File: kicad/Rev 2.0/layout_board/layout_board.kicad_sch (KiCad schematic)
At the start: 144 parts, among them U0:0 GH39FKSW, U0:1 GH39FKSW, U0:10 GH39FKSW, U0:11 GH39FKSW, U0:12 GH39FKSW, U0:13 GH39FKSW, U0:14 GH39FKSW, U0:2 GH39FKSW, U0:3 GH39FKSW, U0:4 GH39FKSW, U0:5 GH39FKSW, U0:6 GH39FKSW, U0:7 GH39FKSW, U0:8 GH39FKSW, U0:9 GH39FKSW, U1 CD4067BPWR, U1:0 GH39FKSW, U1:1 GH39FKSW, U1:10 GH39FKSW, U1:11 GH39FKSW, U1:12 GH39FKSW, U1:13 GH39FKSW, U1:14 GH39FKSW, U1:2 GH39FKSW, U1:3 GH39FKSW, U1:4 GH39FKSW, U1:5 GH39FKSW, U1:6 GH39FKSW, U1:7 GH39FKSW, U1:8 GH39FKSW, U1:9 GH39FKSW, U2 CD4067BPWR, U2:0 GH39FKSW, U2:1 GH39FKSW, U2:10 GH39FKSW, U2:11 GH39FKSW, U2:12 GH39FKSW, U2:13 GH39FKSW, U2:2 GH39FKSW, U2:3 GH39FKSW, U2:4 GH39FKSW, U2:5 GH39FKSW, U2:6 GH39FKSW, U2:7 GH39FKSW, U2:8 GH39FKSW, U2:9 GH39FKSW, U3 CD4067BPWR, U3:1 GH39FKSW, U3:10 GH39FKSW, U3:11 GH39FKSW, U3:12 GH39FKSW, U3:13 GH39FKSW, U3:2 GH39FKSW, U3:3 GH39FKSW, U3:4 GH39FKSW, U3:5 GH39FKSW, U3:6 GH39FKSW, U3:7 GH39FKSW, U3:8 GH39FKSW, U3:9 GH39FKSW, U4 CD4067BPWR, U4:1 GH39FKSW, U4:10 GH39FKSW, U4:12 GH39FKSW, U4:13 GH39FKSW, U4:14 GH39FKSW, U4:2 GH39FKSW, U4:3 GH39FKSW, U4:5 GH39FKSW, U4:7 GH39FKSW, U4:9 GH39FKSW, U5 CD4067BPWR

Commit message: wip: rev 2.0 pcb
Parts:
- removed C1, C10, C11, C12, C13, C14, C15, C16, C17, C18, C19, C2, C20, C21, C22, C23, C24, C25, C26, C27, C28, C29, C3, C30, C31, C32, C33, C34, C35, C36, C37, C38, C39, C4, C40, C41, C42, C43, C44, C45, C46, C47, C48, C49, C5, C50, C51, C52, C53, C54, C55, C56, C57, C58, C59, C6, C60, C61, C62, C63, C64, C65, C66, C67, C7, C8, C9: 100n, Capacitor_SMD:C_0402_1005Metric_Pad0.74x0.62mm_HandSolder, symbol Device:C
- added J1: Conn_01x12_Socket, symbol Connector:Conn_01x12_Socket
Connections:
- net +3.3VA: now also J1.11 (Pin_11)
- net ADC0: now also J1.10 (Pin_10)
- net ADC1: now also J1.9 (Pin_9)
- net ADC2: now also J1.8 (Pin_8)
- net ADC3: now also J1.7 (Pin_7)
- net ADC4: now also J1.6 (Pin_6)
- net AMUX0:0: now also U3:1.2 (VOUT)
- net AMUX0:1: now also U2:1.2 (VOUT)
- net AMUX0:10: now also U0:0.2 (VOUT)
- net AMUX0:11: now also U1:0.2 (VOUT)
- net AMUX0:12: now also U2:0.2 (VOUT)
- net AMUX0:13: now also U4:1.2 (VOUT)
- net AMUX0:2: now also U3:2.2 (VOUT)
- net AMUX0:3: now also U4:2.2 (VOUT)
- net AMUX0:4: now also U2:2.2 (VOUT)
- net AMUX0:5: now also U1:2.2 (VOUT)
- net AMUX0:6: now also U0:3.2 (VOUT)
- net AMUX0:7: now also U0:2.2 (VOUT)
- net AMUX0:8: now also U1:1.2 (VOUT)
- net AMUX0:9: now also U0:1.2 (VOUT)
- net GND: now also J1.12 (Pin_12)
- net SELECT0: now also J1.4 (Pin_4)
- net SELECT1: now also J1.3 (Pin_3)
- net SELECT2: now also J1.2 (Pin_2)
- net SELECT3: now also J1.1 (Pin_1)
- net AMUX0:14: no longer names the net of U1.17 (14)
- net AMUX0:15: no longer names the net of U1.16 (15)
- net AMUX1:13: no longer names the net of U2.18 (13)
- net AMUX1:14: no longer names the net of U2.17 (14)
- net AMUX1:15: no longer names the net of U2.16 (15)
- net AMUX2:13: no longer names the net of U3.18 (13)
- net AMUX2:14: no longer names the net of U3.17 (14)
- net AMUX2:15: no longer names the net of U3.16 (15)
- net AMUX3:13: no longer names the net of U4.18 (13)
- net AMUX3:14: no longer names the net of U4.17 (14)
- net AMUX3:15: no longer names the net of U4.16 (15)
- net AMUX4:14: no longer names the net of U5.17 (14)
- net AMUX4:15: no longer names the net of U5.16 (15)
- no-connect marks 0 -> 13

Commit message: wip: rev 2.0 pcb
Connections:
- net AMUX0:0: now also U0:1.2 (VOUT); no longer U3:1.2 (VOUT)
- net AMUX0:1: now also U0:0.2 (VOUT); no longer U2:1.2 (VOUT)
- net AMUX0:10: now also U1:2.2 (VOUT); no longer U0:0.2 (VOUT)
- net AMUX0:11: now also U2:2.2 (VOUT); no longer U1:0.2 (VOUT)
- net AMUX0:12: now also U0:3.2 (VOUT); no longer U2:0.2 (VOUT)
- net AMUX0:13: now also U0:2.2 (VOUT); no longer U4:1.2 (VOUT)
- net AMUX0:2: now also U1:0.2 (VOUT); no longer U3:2.2 (VOUT)
- net AMUX0:3: now also U2:0.2 (VOUT); no longer U4:2.2 (VOUT)
- net AMUX0:4: now also U4:1.2 (VOUT); no longer U2:2.2 (VOUT)
- net AMUX0:5: now also U3:1.2 (VOUT); no longer U1:2.2 (VOUT)
- net AMUX0:6: now also U2:1.2 (VOUT); no longer U0:3.2 (VOUT)
- net AMUX0:7: now also U1:1.2 (VOUT); no longer U0:2.2 (VOUT)
- net AMUX0:8: now also U3:2.2 (VOUT); no longer U1:1.2 (VOUT)
- net AMUX0:9: now also U4:2.2 (VOUT); no longer U0:1.2 (VOUT)
- net AMUX1:0: now also U0:4.2 (VOUT)
- net AMUX1:1: now also U3:3.2 (VOUT)
- net AMUX1:10: now also U1:5.2 (VOUT)
- net AMUX1:11: now also U2:5.2 (VOUT)
- net AMUX1:12: now also U0:5.2 (VOUT)
- net AMUX1:2: now also U1:3.2 (VOUT)
- net AMUX1:3: now also U2:3.2 (VOUT)
- net AMUX1:4: now also U4:3.2 (VOUT)
- net AMUX1:5: now also U3:4.2 (VOUT)
- net AMUX1:6: now also U2:4.2 (VOUT)
- net AMUX1:7: now also U1:4.2 (VOUT)
- net AMUX1:8: now also U3:5.2 (VOUT)
- net AMUX1:9: now also U4:5.2 (VOUT)
- net AMUX2:0: now also U0:7.2 (VOUT)
- net AMUX2:1: now also U0:6.2 (VOUT)
- net AMUX2:10: now also U1:8.2 (VOUT)
- net AMUX2:11: now also U2:8.2 (VOUT)
- net AMUX2:12: now also U0:8.2 (VOUT)
- net AMUX2:2: now also U3:6.2 (VOUT)
- net AMUX2:3: now also U1:6.2 (VOUT)
- net AMUX2:4: now also U2:6.2 (VOUT)
- net AMUX2:5: now also U3:7.2 (VOUT)
- net AMUX2:6: now also U2:7.2 (VOUT)
- net AMUX2:7: now also U1:7.2 (VOUT)
- net AMUX2:8: now also U3:8.2 (VOUT)
- net AMUX2:9: now also U4:7.2 (VOUT)
- net AMUX3:0: now also U0:10.2 (VOUT)
- net AMUX3:1: now also U0:9.2 (VOUT)
- net AMUX3:10: now also U4:10.2 (VOUT)
- net AMUX3:11: now also U1:11.2 (VOUT)
- net AMUX3:12: now also U0:11.2 (VOUT)
- net AMUX3:2: now also U3:9.2 (VOUT)
- net AMUX3:3: now also U1:9.2 (VOUT)
- net AMUX3:4: now also U2:9.2 (VOUT)
- net AMUX3:5: now also U4:9.2 (VOUT)
- net AMUX3:6: now also U3:10.2 (VOUT)
- net AMUX3:7: now also U1:10.2 (VOUT)
- net AMUX3:8: now also U2:10.2 (VOUT)
- net AMUX3:9: now also U3:11.2 (VOUT)
- net AMUX4:0: now also U0:13.2 (VOUT)
- net AMUX4:1: now also U0:12.2 (VOUT)
- net AMUX4:10: now also U3:13.2 (VOUT)
- net AMUX4:11: now also U4:14.2 (VOUT)
- net AMUX4:12: now also U1:14.2 (VOUT)
- net AMUX4:13: now also U0:14.2 (VOUT)
- net AMUX4:2: now also U2:11.2 (VOUT)
- net AMUX4:3: now also U3:12.2 (VOUT)
- net AMUX4:4: now also U1:12.2 (VOUT)
- net AMUX4:5: now also U2:12.2 (VOUT)
- net AMUX4:6: now also U4:12.2 (VOUT)
- net AMUX4:7: now also U2:13.2 (VOUT)
- net AMUX4:8: now also U1:13.2 (VOUT)
- net AMUX4:9: now also U4:13.2 (VOUT)

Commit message: wip: working on flex cable
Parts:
- added C3, C4: 1u, Capacitor_SMD:C_0402_1005Metric_Pad0.74x0.62mm_HandSolder, symbol Device:C
- added FB2: 120R, Inductor_SMD:L_0603_1608Metric_Pad1.05x0.95mm_HandSolder, symbol Device:FerriteBead
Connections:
- net +3.3VA: now also C4.1, FB2.2
- net GND: now also J1.5 (Pin_5), C3.2, C4.2
- new net +3.3V: C3.1, FB2.1

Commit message: wip: flex connector
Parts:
- removed C3, C4: 1u, Capacitor_SMD:C_0402_1005Metric_Pad0.74x0.62mm_HandSolder, symbol Device:C
- removed FB2: 120R, Inductor_SMD:L_0603_1608Metric_Pad1.05x0.95mm_HandSolder, symbol Device:FerriteBead
- J1: value Conn_01x12_Socket -> Conn_01x11_Socket; footprint (none) -> Custom:Flex Cable connector; symbol Connector:Conn_01x12_Socket -> Connector:Conn_01x11_Socket
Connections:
- net +3.3VA: now also J1.5 (Pin_5); no longer J1.11 (Pin_11)
- net GND: now also J1.11 (Pin_11); no longer J1.12 (Pin_12), J1.5 (Pin_5)

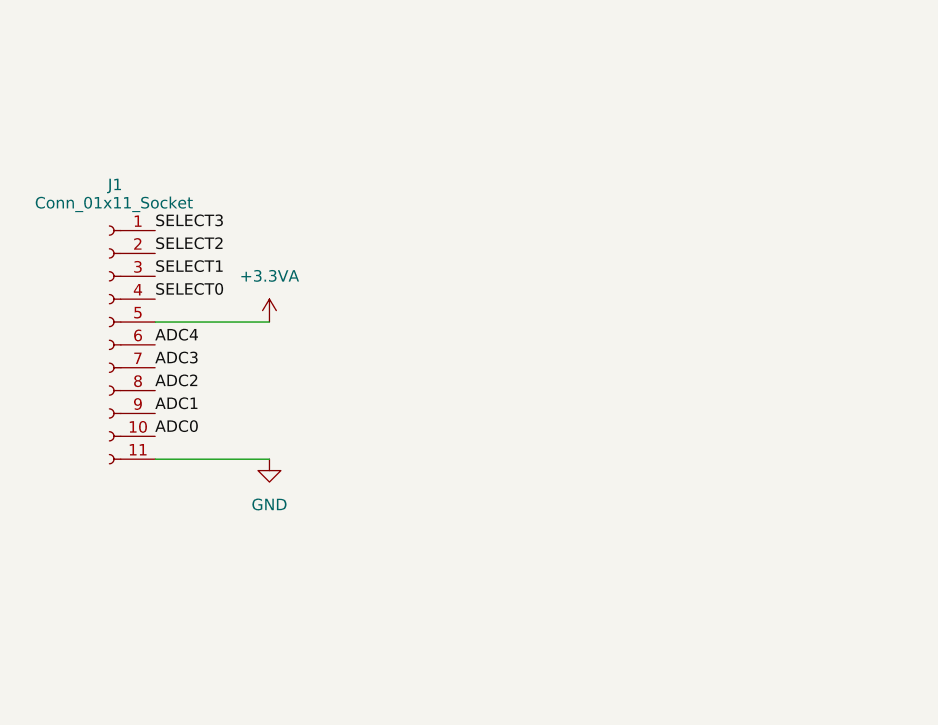
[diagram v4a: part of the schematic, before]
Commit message: wip: remove flex pcb
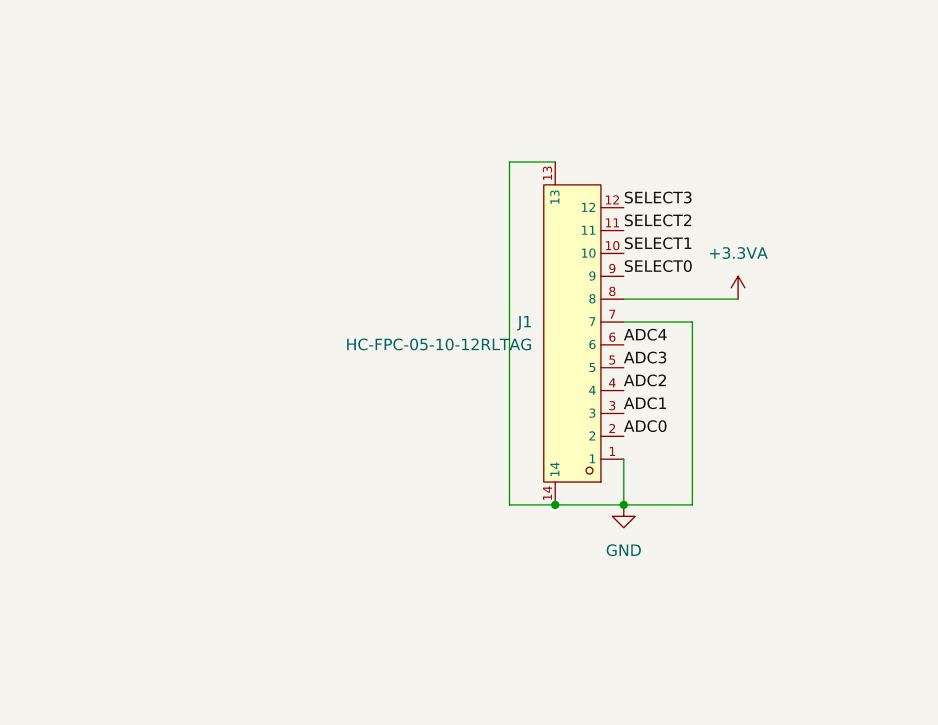
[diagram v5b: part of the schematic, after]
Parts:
- removed J1: Conn_01x11_Socket, Custom:Flex Cable connector, symbol Connector:Conn_01x11_Socket
- added J1: HC-FPC-05-10-12RLTAG, JLCPCB:FPC-SMD_12P-P0.50_HCTL_HC-FPC-05-10-12RLTAG, symbol JLCPCB:HC-FPC-05-10-12RLTAG
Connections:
- net +3.3VA: now also J1.8
- net ADC0: now also J1.2
- net ADC1: now also J1.3
- net ADC2: now also J1.4
- net ADC3: now also J1.5
- net ADC4: now also J1.6
- net GND: now also J1.1, J1.13, J1.14, J1.7
- net SELECT0: now also J1.9
- net SELECT1: now also J1.10
- net SELECT2: now also J1.11
- net SELECT3: now also J1.12

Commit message: wip: changing amuxes
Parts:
- U1, U2, U3, U4, U5: footprint JLCPCB:TSSOP-24_L7.8-W4.4-P0.65-LS6.4-BL_1 -> Custom:(T_S)SOP-24_5.3x8.2mm_P0.65mm
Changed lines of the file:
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@@
 	(wire
 		(pts
-			(xy 157.48 304.8) (xy 168.91 304.8)
-		)
-		(stroke
-			(width 0)
-			(type default)
-		)
-	)
-	(wire
-		(pts
 			(xy 398.78 337.82) (xy 398.78 327.66)
 		)
@@
 	(wire
 		(pts
+			(xy 157.48 304.8) (xy 168.91 304.8)
+		)
+		(stroke
+			(width 0)
+			(type default)
+		)
+	)
+	(wire
+		(pts
 			(xy 237.49 118.11) (xy 237.49 120.65)
 		)
@@
 			)
 		)
-		(property "Footprint" "JLCPCB:TSSOP-24_L7.8-W4.4-P0.65-LS6.4-BL_1"
+		(property "Footprint" "Custom:(T_S)SOP-24_5.3x8.2mm_P0.65mm"
 			(at 443.23 316.23 0)
 			(effects
@@
 			)
 		)
-		(property "Datasheet" "https://www.lcsc.com/datasheet/lcsc_datasheet_2410010330_Texas-Instruments-CD4067BPWR_C2861251.pdf"
+		(property "Datasheet" "https://www.ti.com/lit/ds/symlink/cd4067b.pdf?ts=1733023216324"
 			(at 440.944 305.943 0)
 			(effects
@@
 			)
 		)
-		(property "Footprint" "JLCPCB:TSSOP-24_L7.8-W4.4-P0.65-LS6.4-BL_1"
+		(property "Footprint" "Custom:(T_S)SOP-24_5.3x8.2mm_P0.65mm"
 			(at 367.03 316.23 0)
 			(effects
@@
 			)
 		)
-		(property "Datasheet" "https://www.lcsc.com/datasheet/lcsc_datasheet_2410010330_Texas-Instruments-CD4067BPWR_C2861251.pdf"
+		(property "Datasheet" "https://www.ti.com/lit/ds/symlink/cd4067b.pdf?ts=1733023216324"
 			(at 364.744 305.943 0)
 			(effects
@@
 			)
 		)
-		(property "Footprint" "JLCPCB:TSSOP-24_L7.8-W4.4-P0.65-LS6.4-BL_1"
+		(property "Footprint" "Custom:(T_S)SOP-24_5.3x8.2mm_P0.65mm"
 			(at 137.16 316.23 0)
 			(effects
@@
 			)
 		)
-		(property "Datasheet" "https://www.lcsc.com/datasheet/lcsc_datasheet_2410010330_Texas-Instruments-CD4067BPWR_C2861251.pdf"
+		(property "Datasheet" "https://www.ti.com/lit/ds/symlink/cd4067b.pdf?ts=1733023216324"
 			(at 134.874 305.943 0)
 			(effects
@@
 			)
 		)
-		(property "Footprint" "JLCPCB:TSSOP-24_L7.8-W4.4-P0.65-LS6.4-BL_1"
+		(property "Footprint" "Custom:(T_S)SOP-24_5.3x8.2mm_P0.65mm"
 			(at 213.36 316.23 0)
 			(effects
@@
 			)
 		)
-		(property "Datasheet" "https://www.lcsc.com/datasheet/lcsc_datasheet_2410010330_Texas-Instruments-CD4067BPWR_C2861251.pdf"
+		(property "Datasheet" "https://www.ti.com/lit/ds/symlink/cd4067b.pdf?ts=1733023216324"
 			(at 211.074 305.943 0)
 			(effects
@@
 			)
 		)
-		(property "Footprint" "JLCPCB:TSSOP-24_L7.8-W4.4-P0.65-LS6.4-BL_1"
+		(property "Footprint" "Custom:(T_S)SOP-24_5.3x8.2mm_P0.65mm"
 			(at 289.56 316.23 0)
 			(effects
@@
 			)
 		)
-		(property "Datasheet" "https://www.lcsc.com/datasheet/lcsc_datasheet_2410010330_Texas-Instruments-CD4067BPWR_C2861251.pdf"
+		(property "Datasheet" "https://www.ti.com/lit/ds/symlink/cd4067b.pdf?ts=1733023216324"
 			(at 287.274 305.943 0)
 			(effects

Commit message: release: Rev 2.0 sent to be manufactured
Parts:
- U0:0, U0:1, U0:10, U0:11, U0:12, U0:13, U0:14, U0:2, U0:3, U0:4, U0:5, U0:6, U0:7, U0:8, U0:9, U1:0, U1:1, U1:10, U1:11, U1:12, U1:13, U1:14, U1:2, U1:3, U1:4, U1:5, U1:6, U1:7, U1:8, U1:9, U2:0, U2:1, U2:10, U2:11, U2:12, U2:13, U2:2, U2:3, U2:4, U2:5, U2:6, U2:7, U2:8, U2:9, U3:1, U3:10, U3:11, U3:12, U3:13, U3:2, U3:3, U3:4, U3:5, U3:6, U3:7, U3:8, U3:9, U4:1, U4:10, U4:12, U4:13, U4:14, U4:2, U4:3, U4:5, U4:7, U4:9: footprint JLCPCB:SOT-23-3_L2.9-W1.3-P1.90-LS2.4-BR -> Package_TO_SOT_SMD:SOT-23
- U1, U2, U3, U4, U5: footprint Custom:(T_S)SOP-24_5.3x8.2mm_P0.65mm -> Package_SO:SSOP-24_5.3x8.2mm_P0.65mm
